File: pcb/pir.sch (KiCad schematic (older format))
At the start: 0 parts

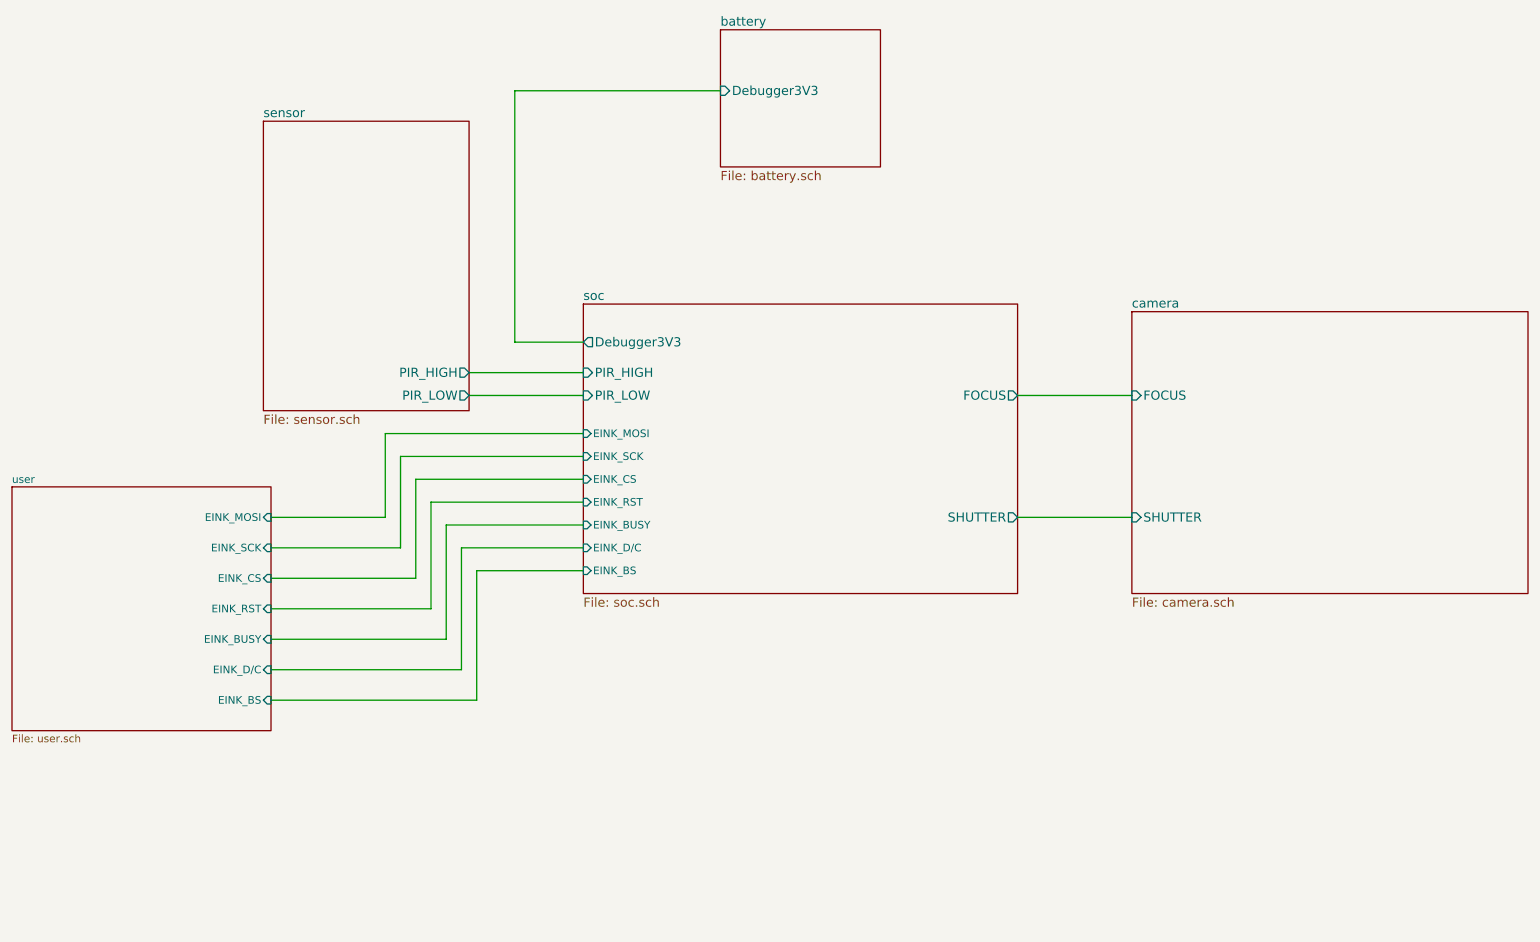
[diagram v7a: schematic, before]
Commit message: MCU change, again
STM32L0 had quite a big problem, common reference for the comparators.
Another minus was the missing SWO for debugging.

STM32L4 has floating point, and most importantly, has embedded OPAMPS!
This means I can directly plug in the filter to the analog inputs and
everything is software. 2 opamps and 2 comparators (if needed).
External circuitry would be minimal for the PIR sensor.

It also means that I can read with the embedded 12-bit ADC the
amplified values. Precision is not crucial, we are interested in dips
and swells.
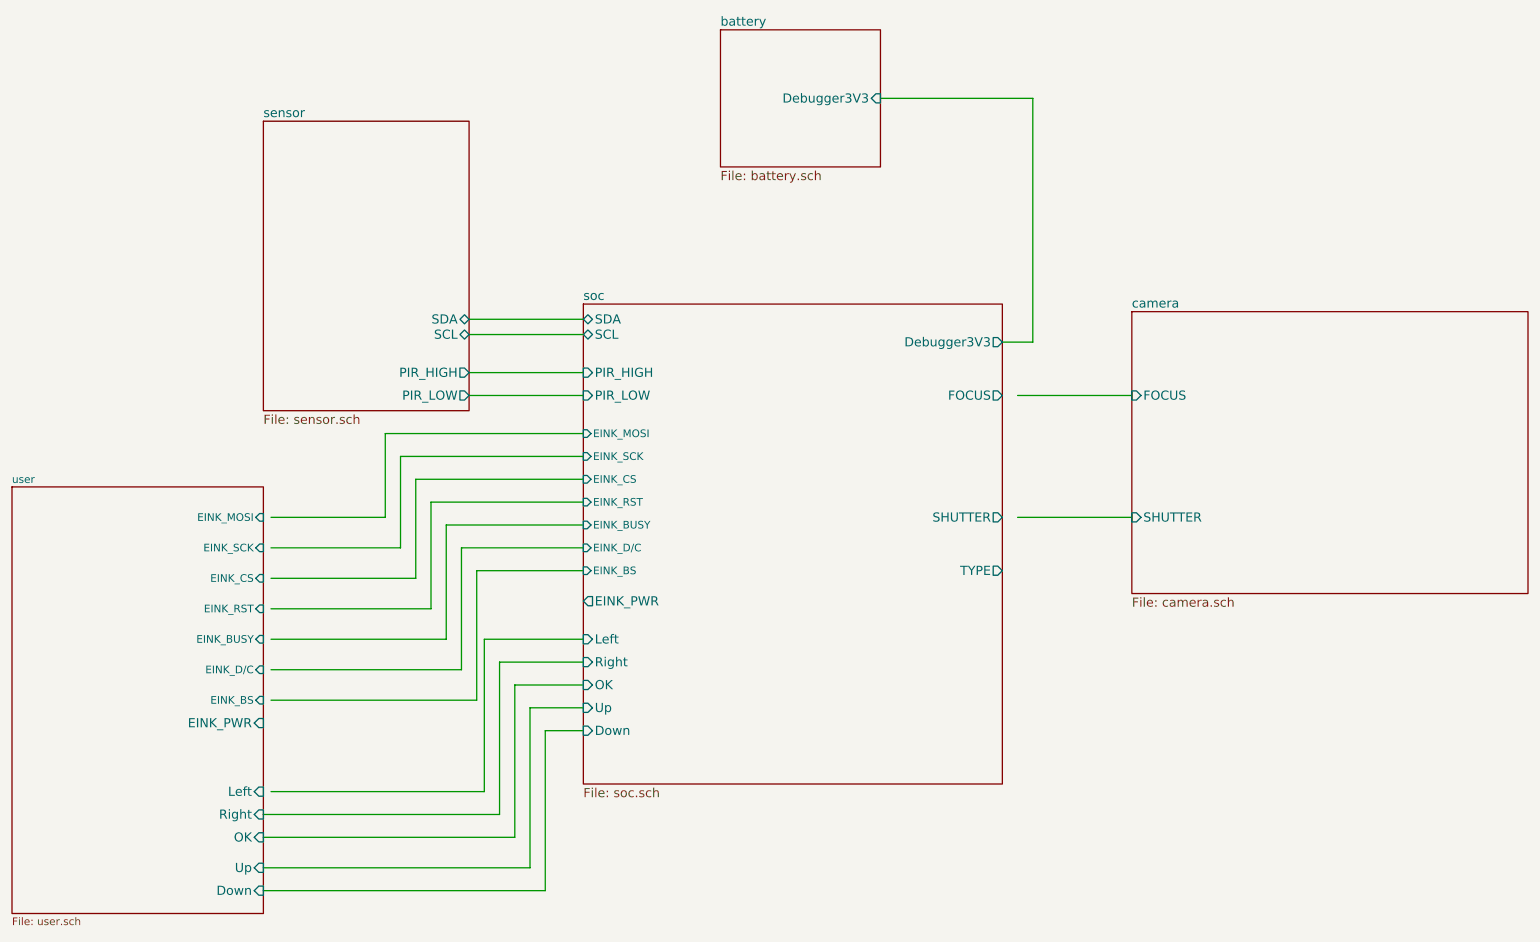
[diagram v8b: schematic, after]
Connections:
- wire segments 28 -> 45
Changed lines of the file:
@@
 EESchema Schematic File Version 2
+LIBS:74xgxx
+LIBS:74xx
+LIBS:Altera
+LIBS:ESD_Protection
+LIBS:LEM
+LIBS:Lattice
+LIBS:Oscillators
+LIBS:Power_Management
+LIBS:RFSolutions
+LIBS:Worldsemi
+LIBS:Xicor
+LIBS:Zilog
+LIBS:ac-dc
+LIBS:actel
+LIBS:adc-dac
+LIBS:allegro
+LIBS:analog_devices
+LIBS:analog_switches
+LIBS:atmel
+LIBS:audio
+LIBS:battery_management
+LIBS:bbd
+LIBS:bosch
+LIBS:brooktre
+LIBS:cmos4000
+LIBS:cmos_ieee
+LIBS:conn
+LIBS:contrib
+LIBS:cypress
+LIBS:dc-dc
+LIBS:device
+LIBS:digital-audio
+LIBS:diode
+LIBS:display
+LIBS:dsp
+LIBS:elec-unifil
+LIBS:ftdi
+LIBS:gennum
+LIBS:graphic_symbols
+LIBS:hc11
+LIBS:infineon
+LIBS:intel
+LIBS:interface
+LIBS:intersil
+LIBS:ir
+LIBS:leds
+LIBS:linear
+LIBS:logic_programmable
+LIBS:maxim
+LIBS:mechanical
+LIBS:memory
+LIBS:microchip
+LIBS:microchip_dspic33dsc
+LIBS:microchip_pic10mcu
+LIBS:microchip_pic12mcu
+LIBS:microchip_pic16mcu
+LIBS:microchip_pic18mcu
+LIBS:microchip_pic24mcu
+LIBS:microchip_pic32mcu
+LIBS:microcontrollers
+LIBS:modules
+LIBS:motor_drivers
+LIBS:motorola
+LIBS:motors
+LIBS:msp430
+LIBS:nordicsemi
+LIBS:nxp
+LIBS:nxp_armmcu
+LIBS:onsemi
+LIBS:opto
+LIBS:philips
 LIBS:power
+LIBS:powerint
+LIBS:pspice
+LIBS:references
+LIBS:regul
+LIBS:relays
+LIBS:rfcom
+LIBS:sensors
+LIBS:silabs
+LIBS:siliconi
+LIBS:stm32
+LIBS:stm8
+LIBS:supertex
+LIBS:switches
+LIBS:texas
+LIBS:transf
+LIBS:transistors
+LIBS:triac_thyristor
+LIBS:ttl_ieee
+LIBS:valves
+LIBS:video
+LIBS:wiznet
+LIBS:xilinx
+LIBS:zetex
+LIBS:SparkFun
+LIBS:ab2_7segment
+LIBS:ab2_audio
+LIBS:ab2_buffer
+LIBS:ab2_capacitor
+LIBS:ab2_connectivity
+LIBS:ab2_dac
+LIBS:ab2_diode
+LIBS:ab2_fuse
+LIBS:ab2_gpio_expansion
+LIBS:ab2_header
+LIBS:ab2_idc
+LIBS:ab2_inductor
+LIBS:ab2_input_devices
+LIBS:ab2_jumper
+LIBS:ab2_lcd
+LIBS:ab2_led
+LIBS:ab2_memory
+LIBS:ab2_opamp
+LIBS:ab2_pinouts
+LIBS:ab2_pot
+LIBS:ab2_power
+LIBS:ab2_regulator
+LIBS:ab2_relay
+LIBS:ab2_resistor
+LIBS:ab2_sensor
+LIBS:ab2_stepper
+LIBS:ab2_supply
+LIBS:ab2_terminal_block
+LIBS:ab2_test
+LIBS:ab2_transistor
+LIBS:ab2_uC
+LIBS:ab2_usb
+LIBS:ab2_xtal
 LIBS:pir-cache
 EELAYER 25 0
@@
 F2 "PIR_HIGH" O R 3800 3400 60
 F3 "PIR_LOW" O R 3800 3550 60
+F4 "SDA" B R 3800 3050 60
+F5 "SCL" B R 3800 3150 60
 $EndSheet
 $Sheet
@@
 F0 "battery" 60
 F1 "battery.sch" 60
-F2 "Debugger3V3" I L 5450 1550 60
-$EndSheet
-$Sheet
-S 4550 2950 2850 1900
+F2 "Debugger3V3" I R 6500 1600 60
+$EndSheet
+$Sheet
+S 4550 2950 2750 3150
 U 5A76AF1D
 F0 "soc" 60
@@
 F2 "PIR_HIGH" I L 4550 3400 60
 F3 "PIR_LOW" I L 4550 3550 60
-F4 "FOCUS" O R 7400 3550 60
-F5 "SHUTTER" O R 7400 4350 60
-F6 "Debugger3V3" O L 4550 3200 60
+F4 "FOCUS" O R 7300 3550 60
+F5 "SHUTTER" O R 7300 4350 60
+F6 "Debugger3V3" O R 7300 3200 60
 F7 "EINK_SCK" I L 4550 3950 50
 F8 "EINK_MOSI" I L 4550 3800 50
@@
 F12 "EINK_D/C" I L 4550 4550 50
 F13 "EINK_BS" I L 4550 4700 50
+F14 "EINK_PWR" O L 4550 4900 60
+F15 "TYPE" O R 7300 4700 60
+F16 "SCL" B L 4550 3150 60
+F17 "SDA" B L 4550 3050 60
+F18 "Left" I L 4550 5150 60
+F19 "Right" I L 4550 5300 60
+F20 "Up" I L 4550 5600 60
+F21 "Down" I L 4550 5750 60
+F22 "OK" I L 4550 5450 60
 $EndSheet
 Wire Wire Line
@@
 Wire Wire Line
 	7400 4350 8150 4350
-Wire Wire Line
-	4100 3200 4550 3200
-Wire Wire Line
-	4100 1550 4100 3200
-Wire Wire Line
-	4100 1550 5450 1550
-$Sheet
-S 800  4150 1700 1600
+$Sheet
+S 800  4150 1650 2800
 U 5A7EC53C
 F0 "user" 50
 F1 "user.sch" 50
-F2 "EINK_MOSI" I R 2500 4350 50
-F3 "EINK_SCK" I R 2500 4550 50
-F4 "EINK_CS" I R 2500 4750 50
-F5 "EINK_RST" I R 2500 4950 50
-F6 "EINK_BUSY" I R 2500 5150 50
-F7 "EINK_D/C" I R 2500 5350 50
-F8 "EINK_BS" I R 2500 5550 50
+F2 "EINK_MOSI" I R 2450 4350 50
+F3 "EINK_SCK" I R 2450 4550 50
+F4 "EINK_CS" I R 2450 4750 50
+F5 "EINK_RST" I R 2450 4950 50
+F6 "EINK_BUSY" I R 2450 5150 50
+F7 "EINK_D/C" I R 2450 5350 50
+F8 "EINK_BS" I R 2450 5550 50
+F9 "EINK_PWR" I R 2450 5700 60
+F10 "Down" I R 2450 6800 60
+F11 "Right" I R 2450 6300 60
+F12 "OK" I R 2450 6450 60
+F13 "Up" I R 2450 6650 60
+F14 "Left" I R 2450 6150 60
 $EndSheet
 Wire Wire Line
@@
 Wire Wire Line
 	2500 5550 3850 5550
+Wire Wire Line
+	6500 1600 7500 1600
+Wire Wire Line
+	7500 1600 7500 3200
+Wire Wire Line
+	7500 3200 7300 3200
+Wire Wire Line
+	3800 3150 4550 3150
+Wire Wire Line
+	4550 3050 3800 3050
+Wire Wire Line
+	2500 6150 3900 6150
+Wire Wire Line
+	3900 6150 3900 5150
+Wire Wire Line
+	3900 5150 4550 5150
+Wire Wire Line
+	2450 6300 4000 6300
+Wire Wire Line
+	4000 6300 4000 5300
+Wire Wire Line
+	4000 5300 4550 5300
+Wire Wire Line
+	2450 6450 4100 6450
+Wire Wire Line
+	4100 6450 4100 5450
+Wire Wire Line
+	4100 5450 4550 5450
+Wire Wire Line
+	2450 6650 4200 6650
+Wire Wire Line
+	4200 6650 4200 5600
+Wire Wire Line
+	4200 5600 4550 5600
+Wire Wire Line
+	2450 6800 4300 6800
+Wire Wire Line
+	4300 6800 4300 5750
+Wire Wire Line
+	4300 5750 4550 5750
 $EndSCHEMATC
